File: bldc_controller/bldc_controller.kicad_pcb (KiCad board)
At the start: 6 copper layers, 69.7 x 76.7 mm, 252 parts, among them J1 XT60PW-M, J10 JST S2B-PH-SM4-TB, J11 Phase A, J12 Phase B, J13 Phase C, J2 XT60PW-M, J3 SM08B-GHS-TB, J4 SM07B-GHS-TB, J5 JST S2B-PH-SM4-TB, J6 SM06B-GHS-TB, J7 Nano-Fit 1x03, J8 Nano-Fit 1x03, J9 SM05B-GHS-TB, Q1 TPH2R408QM,L1Q, Q2 TPH2R408QM,L1Q, Q3 TPH2R408QM,L1Q, Q4 TPH2R408QM,L1Q, Q5 TPH2R408QM,L1Q, Q6 TPH2R408QM,L1Q, Q7 SSM3K324R,LF, SW1 CAS-220TA, U1 SMBJ51CD-M3/H, U10 DRV8353FS, U11 SMBJ51CD-M3/H, U12 LMR36006FSCQRNXRQ1, U13 DGD0216WT-7, U2 MAX15062BATA+T, U3 ADP5301ACBZ-4-R7, U4 LP2992IM5-3.3/NOPB, U5 STM32G474RET3, U6 AS5047P, U7 AS5048B, U8 SN65HVD35DR, U9 TCAN1051HGVDRBRQ1

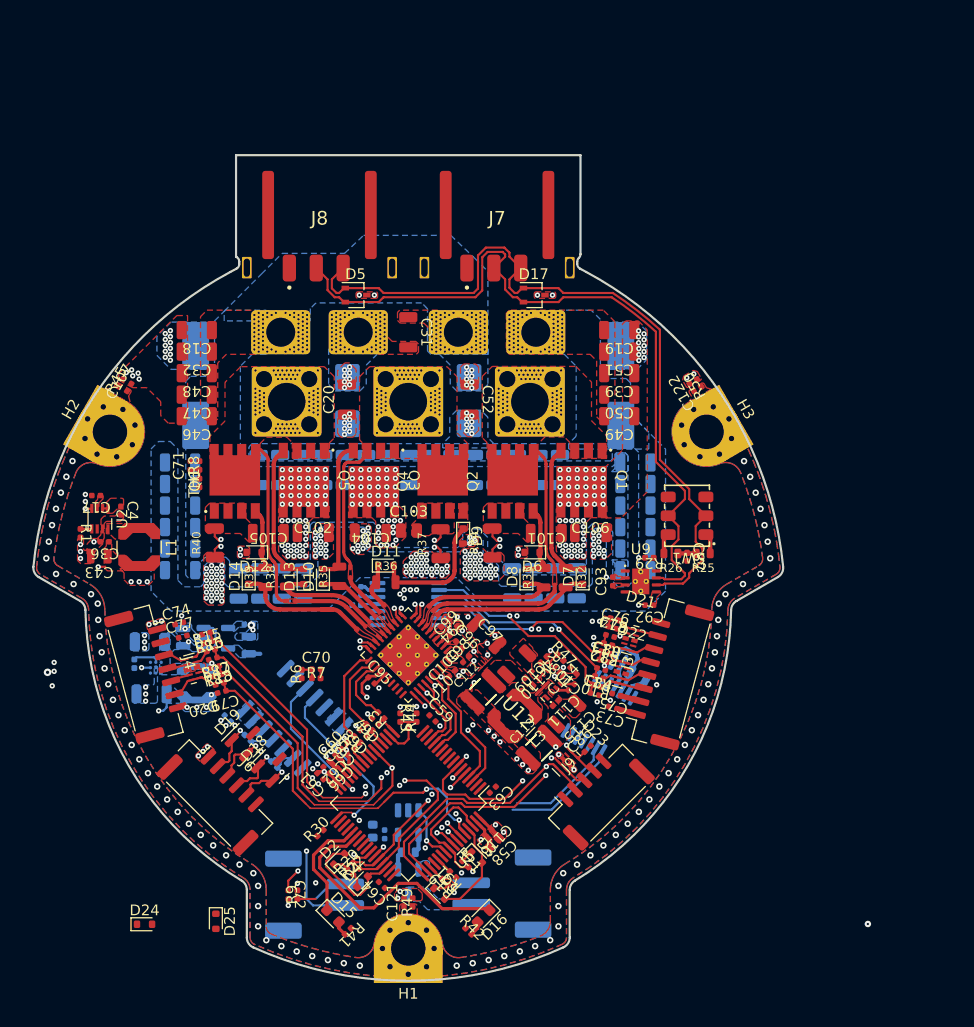
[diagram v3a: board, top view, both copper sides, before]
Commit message: starting rerouting for PCBWay 8/8 mils, 0.25mm drill
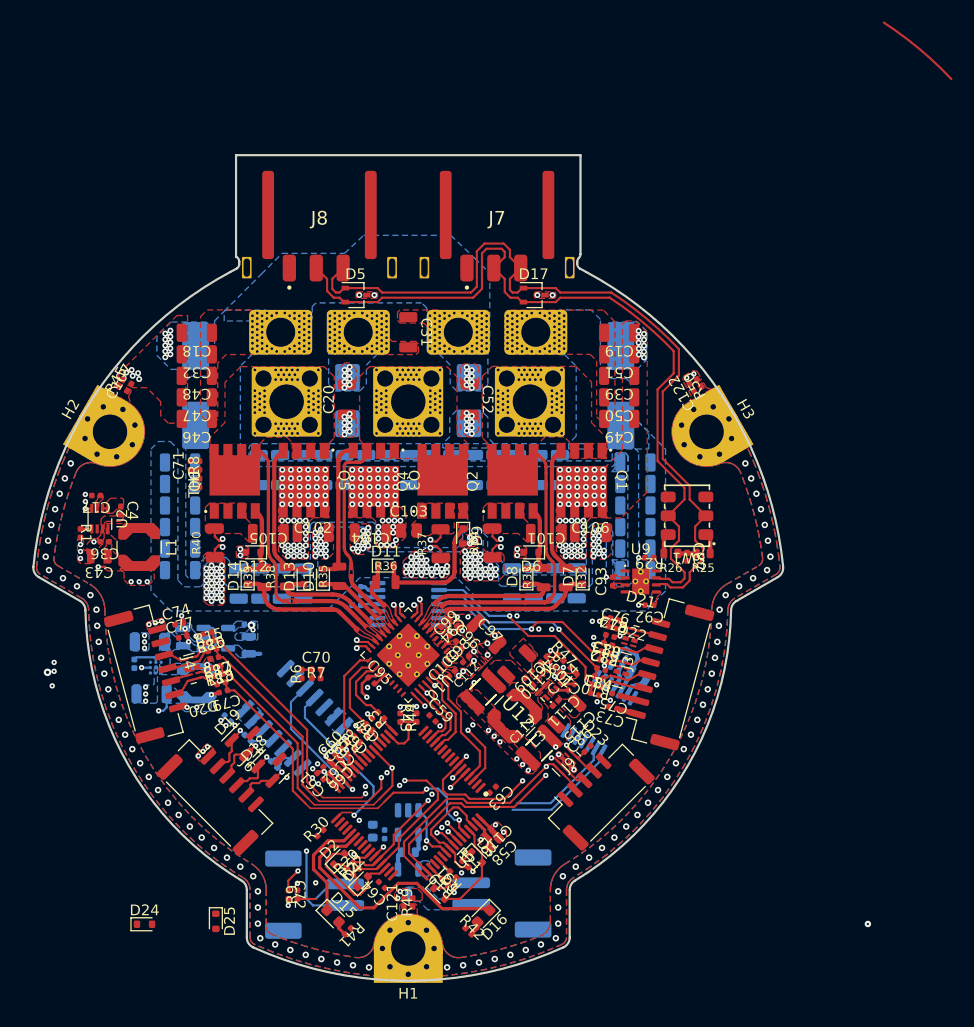
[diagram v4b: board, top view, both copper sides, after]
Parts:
- U10: footprint Package_DFN_QFN:HVQFN-40-1EP_6x6mm_P0.5mm_EP4.1x4.1mm_ThermalVias -> 0_package_DFN_QFN:WQFN-40-1EP_6x6mm_P0.5mm_EP4.15x4.15mm_ThermalVias
- U5: footprint Package_QFP:LQFP-64_10x10mm_P0.5mm -> 0_package_QFP:LQFP-64_10x10mm_P0.5mm
- moved NT6 1.69 mm to (162.7, 87.3), turned to 90 degrees
- moved NT12 1.42 mm to (136.9, 87.0), turned to 90 degrees
- moved NT9 0.83 mm to (144.8, 86.5), turned to 0 degrees
- moved NT13 0.45 mm to (132.1, 93.6), turned to 135 degrees
- moved NT14 0.45 mm to (132.1, 94.4), turned to -135 degrees
- moved NT10 0.41 mm to (152.7, 93.7), turned to 45 degrees
- moved NT8 0.41 mm to (157.9, 94.5), turned to -135 degrees
- moved NT11 0.41 mm to (152.7, 94.5), turned to -45 degrees
- moved NT7 0.41 mm to (157.9, 93.6), turned to -45 degrees
- moved C18 0.25 mm to (130.2, 74.5)
- moved C19 0.25 mm to (169.5, 74.5)
- moved C32 0.25 mm to (130.2, 76.5)
- moved C39 0.25 mm to (169.5, 78.5)
- moved C46 0.25 mm to (130.2, 82.5)
- moved C47 0.25 mm to (130.2, 80.5)
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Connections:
- J10 pad MP: (no net) -> CHASSIS
- J3 pad MP: (no net) -> CHASSIS
- J5 pad MP: (no net) -> CHASSIS
- J6 pad MP: (no net) -> CHASSIS
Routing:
- net GND: track 15.9 -> 22.3 mm, vias 247 -> 240
- net /Project Architecture/Interface - FD-CAN/FDCAN_N: track 72.9 -> 75.2 mm
- net /Project Architecture/Interface - FD-CAN/FDCAN_P: track 72.2 -> 74.4 mm
- net /Project Architecture/Motor Control - Top Level/Motor Control - Inverter/PHA: track 0.00 -> 2.04 mm
- net /Project Architecture/Motor Control - Top Level/Motor Control - Inverter/PHB: track 0.00 -> 1.72 mm
- net /Project Architecture/Motor Control - Top Level/SHC: track 22.5 -> 21.0 mm
- net /Project Architecture/Motor Control - Top Level/Motor Control - Inverter/PHC: track 0.56 -> 1.94 mm
- net /Project Architecture/Motor Control - Top Level/SHA: track 24.0 -> 22.7 mm
- net /Project Architecture/Motor Control - Top Level/Motor Control - Inverter/SRC_LS_C: track 0.00 -> 0.83 mm
- net /Project Architecture/Motor Control - Top Level/Motor Control - Inverter/SRC_LS_B: track 0.00 -> 0.80 mm
- net /Project Architecture/Motor Control - Top Level/Motor Control - Inverter/SRC_LS_A: track 0.00 -> 0.80 mm
- net /Project Architecture/Motor Control - Top Level/SHB: track 16.1 -> 15.3 mm
- net /Project Architecture/Motor Control - Top Level/SA_P: track 16.9 -> 17.5 mm
- net CHASSIS: vias 82 -> 86
- net +VBAT: vias 175 -> 174
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
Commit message: added mousebites, custom footprints and routed some digital/analog parts
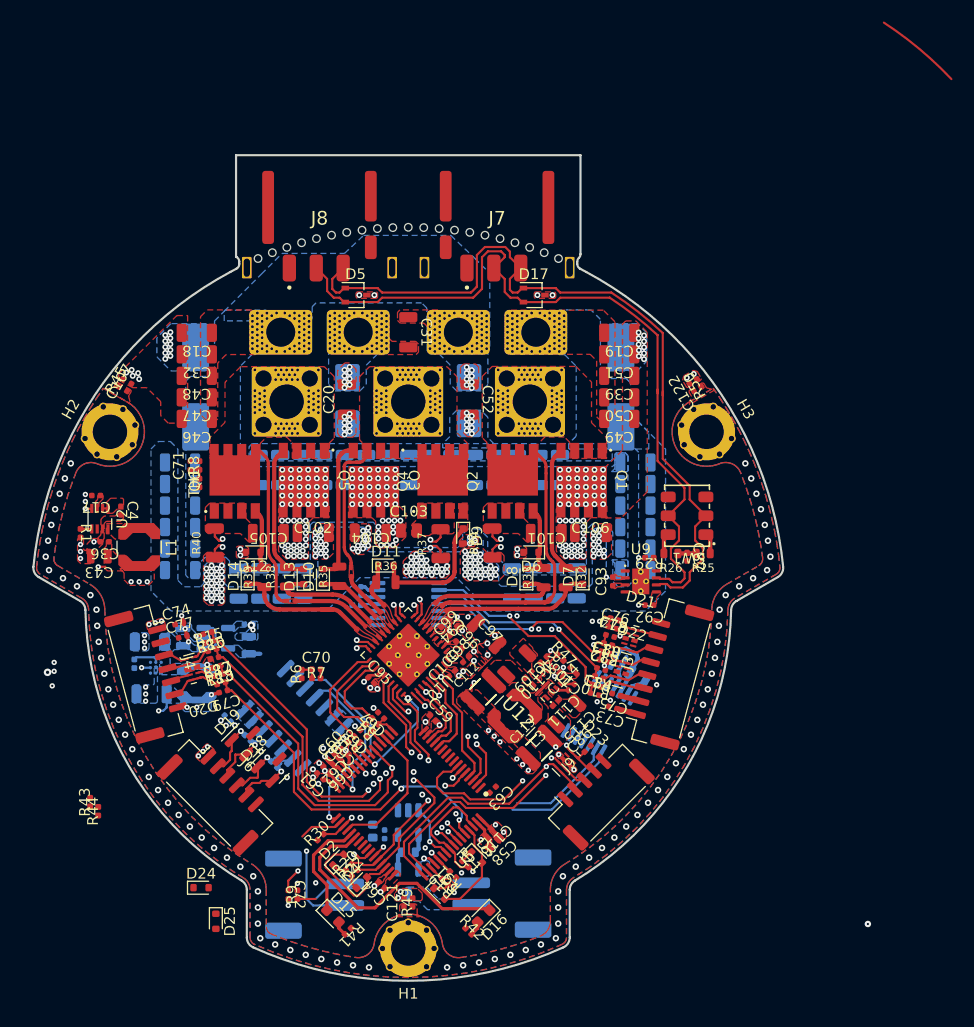
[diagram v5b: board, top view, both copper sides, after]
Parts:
- added REF**: mousebites_single_0.7mm, 0_mousebites:mousebites_single_0.7mm, F.Cu at (138.6, 66.6)
- added REF**: mousebites_single_0.7mm, 0_mousebites:mousebites_single_0.7mm, F.Cu at (135.9, 67.6)
- added REF**: mousebites_single_0.7mm, 0_mousebites:mousebites_single_0.7mm, F.Cu at (144.2, 65.2)
- added REF**: mousebites_single_0.7mm, 0_mousebites:mousebites_single_0.7mm, F.Cu at (140.0, 66.1)
- added REF**: mousebites_single_0.7mm, 0_mousebites:mousebites_single_0.7mm, F.Cu at (145.6, 65.0)
- added REF**: mousebites_single_0.7mm, 0_mousebites:mousebites_single_0.7mm, F.Cu at (152.8, 64.8)
- added REF**: mousebites_single_0.7mm, 0_mousebites:mousebites_single_0.7mm, F.Cu at (151.3, 64.7)
- added REF**: mousebites_single_0.7mm, 0_mousebites:mousebites_single_0.7mm, F.Cu at (159.8, 66.1)
- added REF**: mousebites_single_0.7mm, 0_mousebites:mousebites_single_0.7mm, F.Cu at (158.4, 65.8)
- added REF**: mousebites_single_0.7mm, 0_mousebites:mousebites_single_0.7mm, F.Cu at (161.2, 66.6)
- added REF**: mousebites_single_0.7mm, 0_mousebites:mousebites_single_0.7mm, F.Cu at (157.0, 65.4)
- added REF**: mousebites_single_0.7mm, 0_mousebites:mousebites_single_0.7mm, F.Cu at (162.5, 67.1)
- added REF**: mousebites_single_0.7mm, 0_mousebites:mousebites_single_0.7mm, F.Cu at (154.2, 65.0)
- added REF**: mousebites_single_0.7mm, 0_mousebites:mousebites_single_0.7mm, F.Cu at (147.0, 64.8)
- added REF**: mousebites_single_0.7mm, 0_mousebites:mousebites_single_0.7mm, F.Cu at (148.5, 64.7)
- added REF**: mousebites_single_0.7mm, 0_mousebites:mousebites_single_0.7mm, F.Cu at (163.9, 67.6)
- added REF**: mousebites_single_0.7mm, 0_mousebites:mousebites_single_0.7mm, F.Cu at (141.4, 65.8)
- added REF**: mousebites_single_0.7mm, 0_mousebites:mousebites_single_0.7mm, F.Cu at (137.3, 67.1)
- added REF**: mousebites_single_0.7mm, 0_mousebites:mousebites_single_0.7mm, F.Cu at (155.6, 65.2)
- added REF**: mousebites_single_0.7mm, 0_mousebites:mousebites_single_0.7mm, F.Cu at (142.8, 65.4)
- added REF**: mousebites_single_0.7mm, 0_mousebites:mousebites_single_0.7mm, F.Cu at (149.9, 64.7)
- moved R44 30.8 mm to (121.1, 119.0)
- moved R43 29.9 mm to (120.3, 118.1), turned to 90 degrees
- moved D24 6.25 mm to (130.7, 126.0)
- moved C67 0.78 mm to (147.4, 110.0)
- moved R3 0.78 mm to (146.8, 110.6)
- moved R30 0.38 mm to (141.8, 121.3)
- moved R20 0.18 mm to (144.4, 124.1)
- moved R22 0.18 mm to (144.9, 124.7)
- moved C117 0.15 mm to (169.7, 79.5)
- moved C118 0.15 mm to (130.2, 79.5)
- moved D4 0.11 mm to (145.6, 125.6)
- moved D2 0.11 mm to (143.4, 123.5)
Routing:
- net /Project Architecture/MCU - IO/MOTOR_FAULT: track 0.00 -> 30.9 mm, vias 0 -> 2
- net /Project Architecture/MCU - IO/DRV_MISO: track 1.54 -> 28.5 mm, vias 0 -> 2
- net /Project Architecture/MCU - IO/DRV_SCLK: track 0.00 -> 24.6 mm, vias 0 -> 2
- net /Project Architecture/MCU - IO/DRV_MOSI: track 0.00 -> 15.2 mm, vias 0 -> 2
- net /Project Architecture/Interface - Interconnects/AUX1_A: track 19.3 -> 32.3 mm
- net /Project Architecture/MCU - IO/DRV_CS: track 0.00 -> 9.84 mm, vias 0 -> 2
- net /Project Architecture/MCU - IO/BOARD_VERSION: track 5.94 -> 0.00 mm
- net GND: track 22.3 -> 18.2 mm, vias 240 -> 242
- net /Project Architecture/MCU - IO/SENSE_TEMP_FET: track 1.67 -> 5.71 mm
- net /Project Architecture/Interface - RS-422/RS422_~{RE}: track 13.5 -> 16.0 mm
- net /Project Architecture/MCU - IO/MOTOR_HIZ: track 15.6 -> 17.9 mm
- net /Project Architecture/MCU - IO/SOB: track 7.48 -> 9.34 mm
- net /Project Architecture/Interface - FD-CAN/FDCAN_P: track 74.4 -> 72.8 mm
- net /Project Architecture/Interface - FD-CAN/FDCAN_N: track 75.2 -> 73.7 mm
- net /Project Architecture/Interface - Interconnects/AUX1_E: track 41.9 -> 43.4 mm
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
